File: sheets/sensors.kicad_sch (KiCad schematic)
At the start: 14 parts, among them CN1 StemmaQT, U6 SparkfunM9N, U7 BMP581, U8 ADXL345BCCZ-RL7, U9 ADXL375BCCZ-RL7

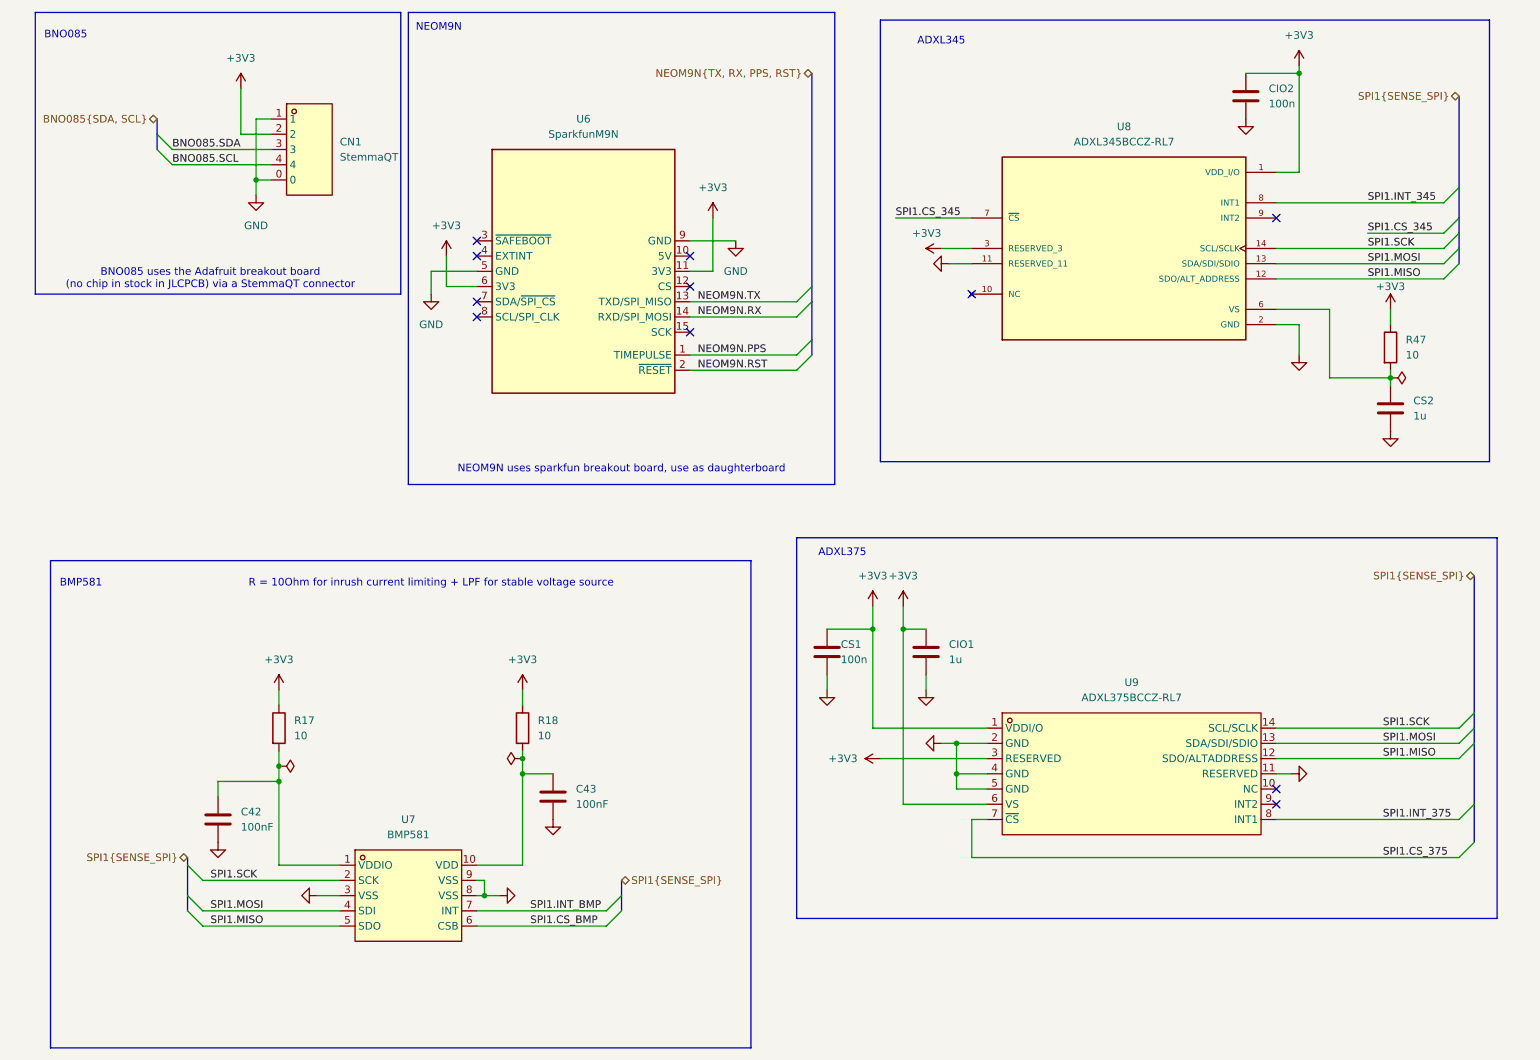
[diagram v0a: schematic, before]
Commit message: solved reverse polarity w pmos and tvs clamp
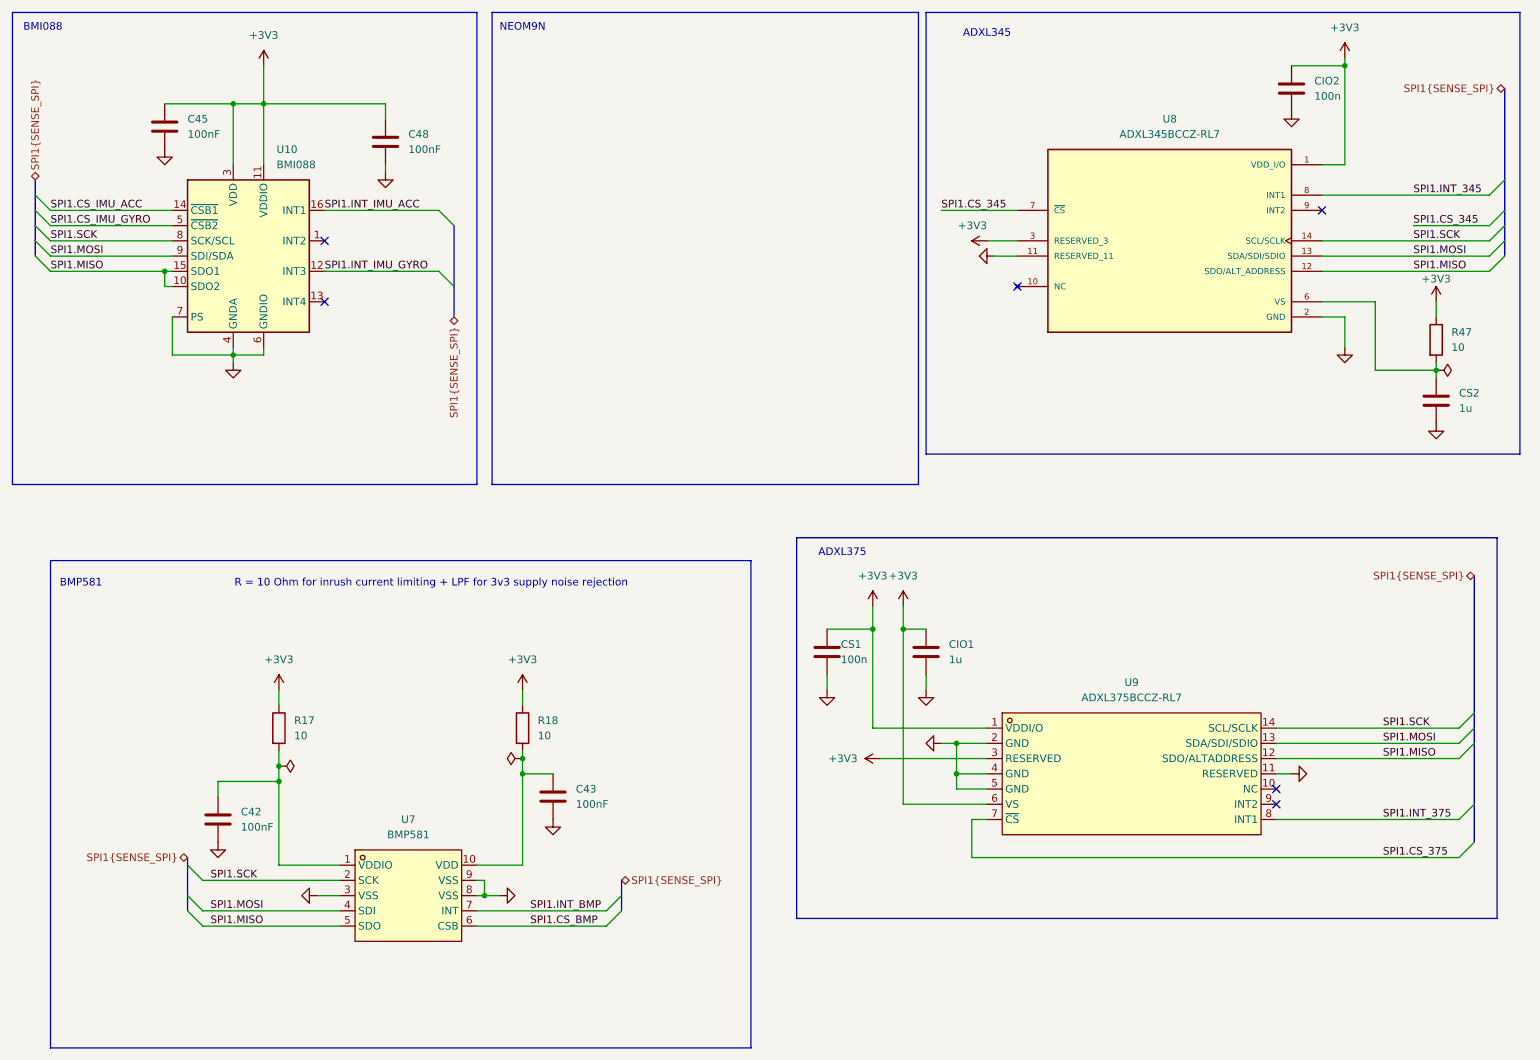
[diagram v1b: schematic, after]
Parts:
- removed CN1: StemmaQT, aerolotl_custom:CONN-SMD_BM04B-SRSS-TB, symbol aerolotl_custom:StemmaQT
- removed U6: SparkfunM9N, RF_GPS:ublox_NEO, symbol aerolotl_custom:SparkfunM9N
- added C45, C48: 100nF, symbol Device:C
- added U10: BMI088, Package_LGA:Bosch_LGA-16_4.5x3mm_P0.5mm_LayoutBorder7x1y_ClockwisePinNumbering, symbol Sensor_Motion:BMI088
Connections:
- net +3V3: now also C45.1, C48.1, U10.11 (VDDIO), U10.3 (VDD)
- net GND: now also C45.2, C48.2, U10.2 (GNDA), U10.4 (GNDA), U10.6 (GNDIO), U10.7 (PS)
- net SPI1.MISO: now also U10.10 (SDO2), U10.15 (SDO1)
- net SPI1.MOSI: now also U10.9 (SDI/SDA)
- net SPI1.SCK: now also U10.8 (SCK/SCL)
- new net SPI1.CS_IMU_ACC: U10.14 (~{CSB1})
- new net SPI1.CS_IMU_GYRO: U10.5 (~{CSB2})
- new net SPI1.INT_IMU_ACC: U10.16 (INT1)
- new net SPI1.INT_IMU_GYRO: U10.12 (INT3)
- no-connect marks 11 -> 6
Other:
- note added: "BMI088"
- note added: "R = 10 Ohm for inrush current limiting + LPF for 3v3 supply noise rejection"
- note removed: "BNO085"
- note removed: "BNO085 uses the Adafruit breakout board (no chip in stock in JLCPCB) via a StemmaQT connector"
- note removed: "NEOM9N uses sparkfun breakout board, use as daughterboard"
- note removed: "R = 10Ohm for inrush current limiting + LPF for stable voltage source"
- moved on the sheet: CIO2, CS2, R47, U8

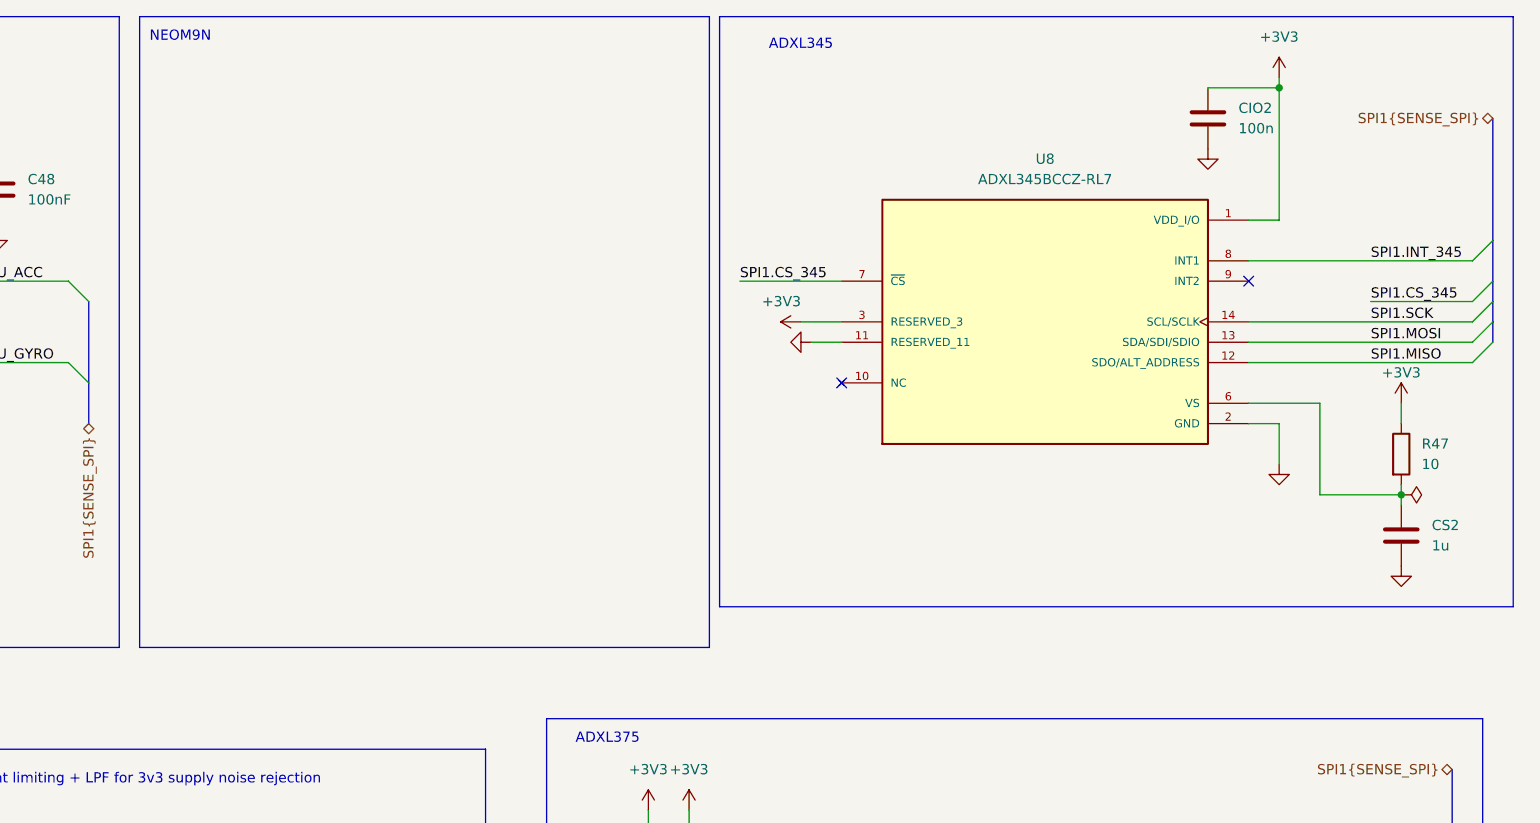
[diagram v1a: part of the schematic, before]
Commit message: replaced bno w bmi
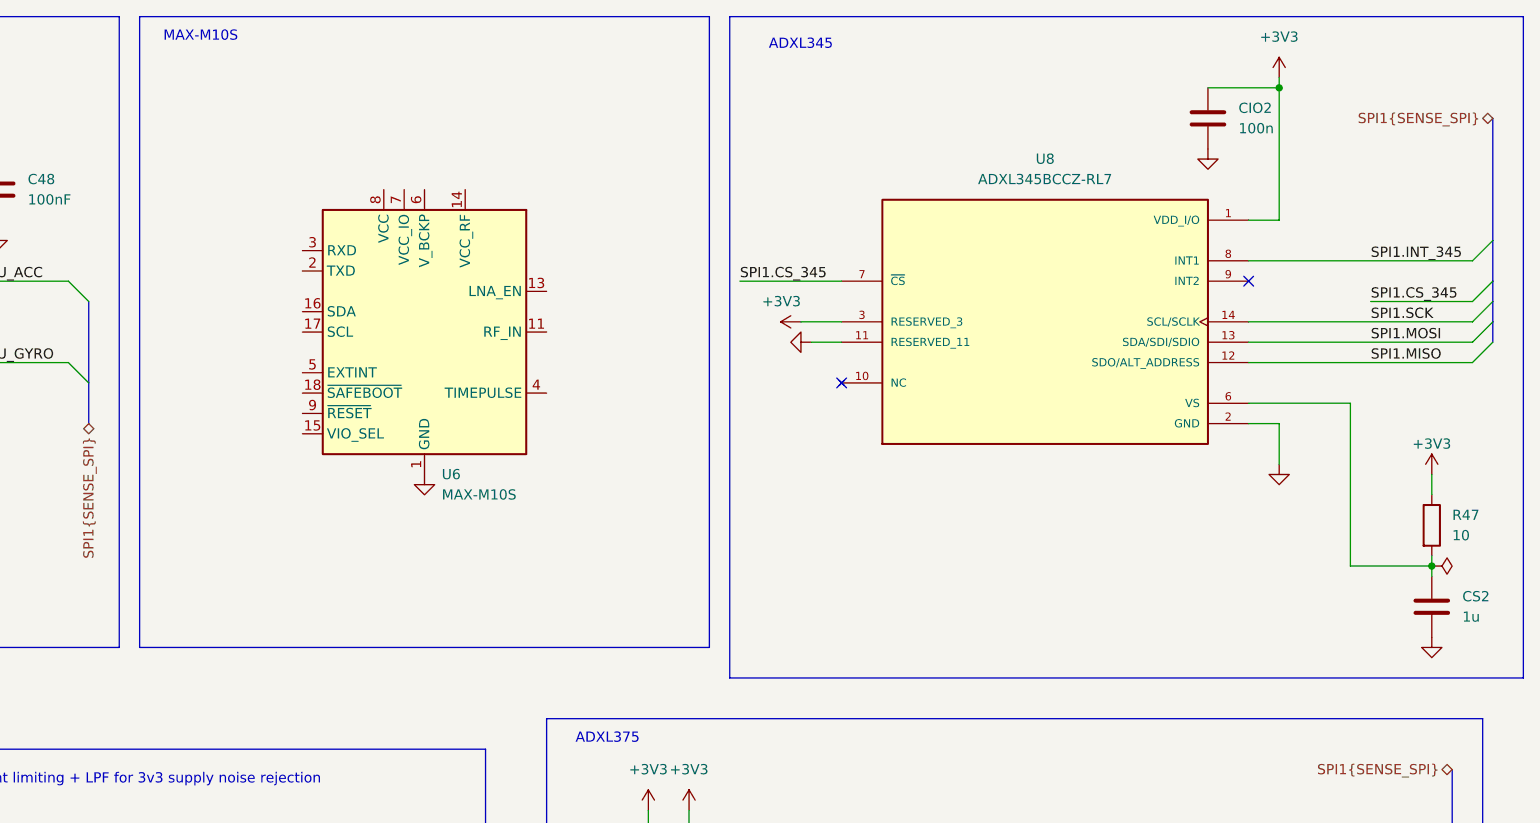
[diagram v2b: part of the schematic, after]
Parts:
- added U6: MAX-M10S, RF_GPS:ublox_MAX, symbol RF_GPS:MAX-M10S
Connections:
- net GND: now also U6.1 (GND), U6.10 (GND), U6.12 (GND)
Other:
- note added: "MAX-M10S"
- note removed: "NEOM9N"
- moved on the sheet: CS2, R47
